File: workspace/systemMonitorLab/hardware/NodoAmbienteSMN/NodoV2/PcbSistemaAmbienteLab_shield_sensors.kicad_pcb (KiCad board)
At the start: 2 copper layers, 32 x 51 mm, 6 parts, among them J5 Molex_Sensor_BMP280, J6 Molex_Sensor_DHT22, U2 Bmp280Module, U3 DHT22

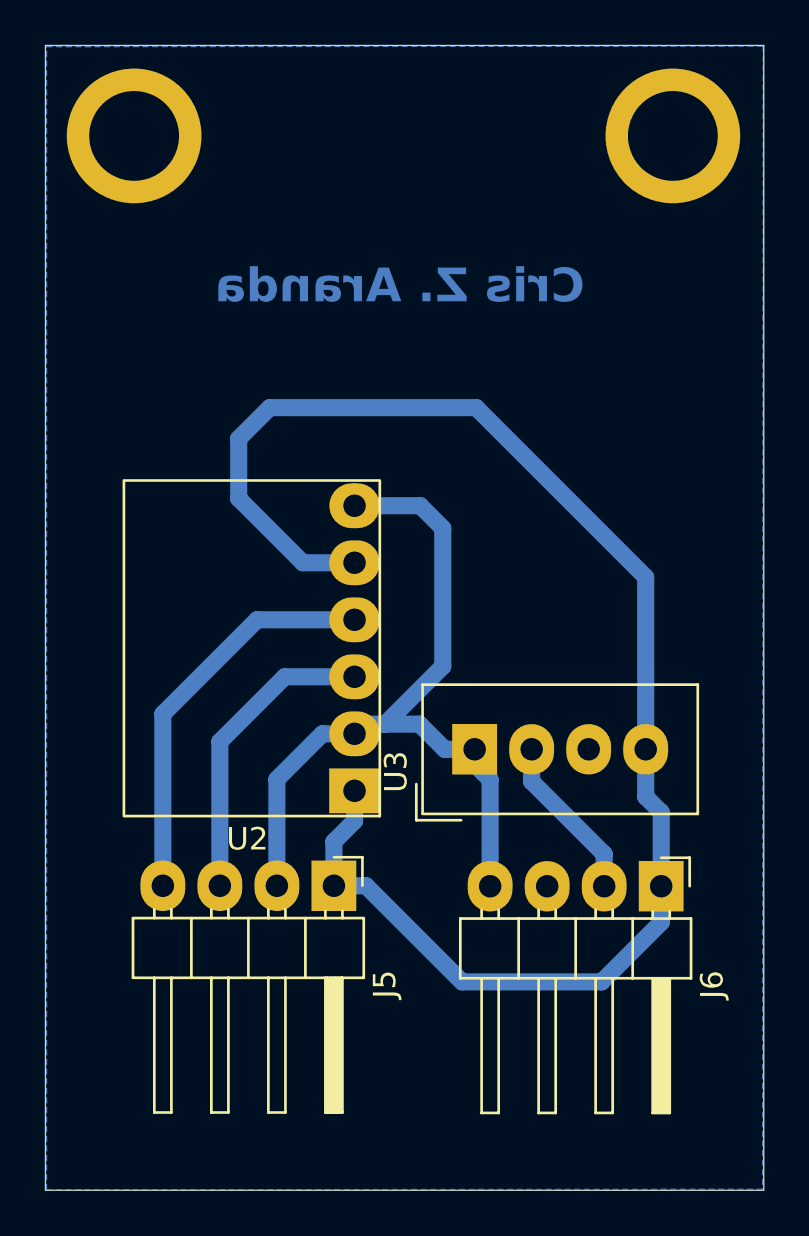
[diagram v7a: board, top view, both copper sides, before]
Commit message: Se mejora el plano de masa del PCB
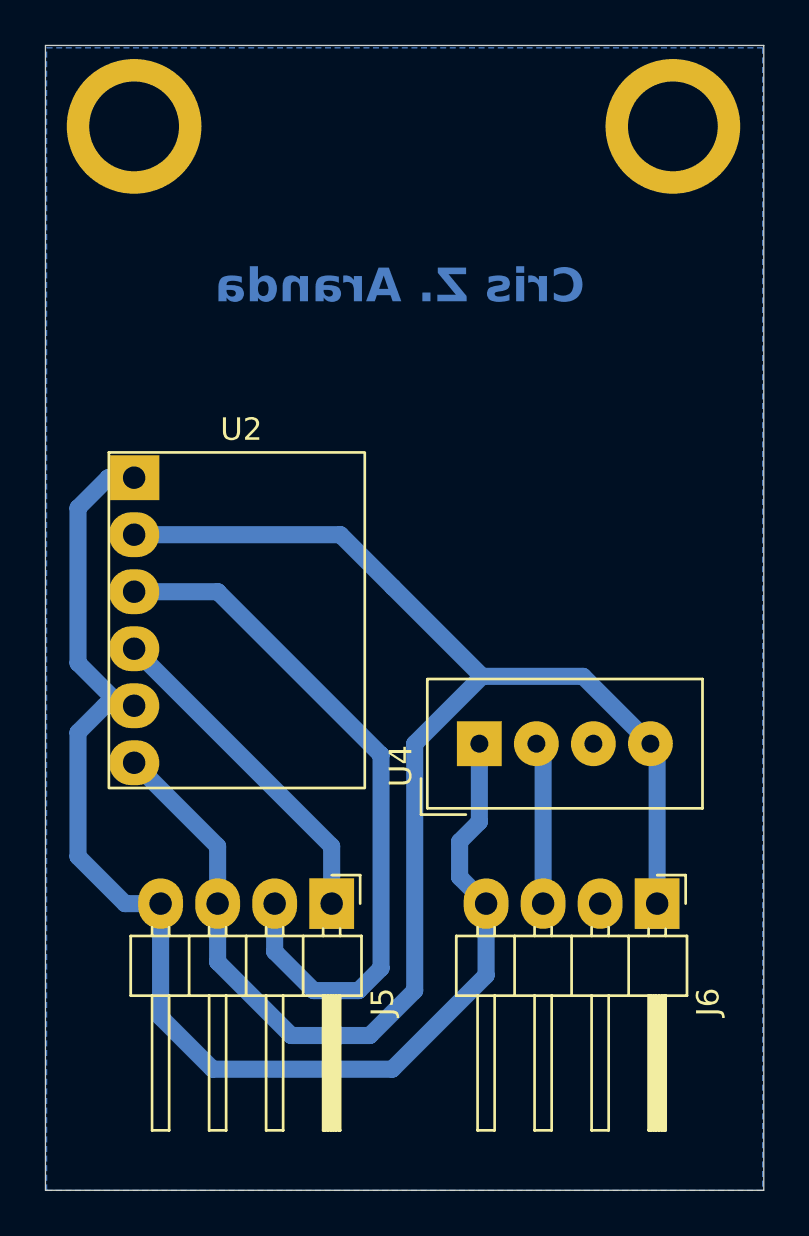
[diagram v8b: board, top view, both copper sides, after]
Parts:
- removed the ? at (180.0, 52.9)
- removed the ? at (156.0, 52.9)
- removed U3: DHT22, Sensor:Aosong_DHT11_5.5x12.0_P2.54mm
- added ?: , , F.Cu at (180.0, 52.5)
- added ?: , , F.Cu at (156.0, 52.5)
- added U4: DHT22, Sensor:Aosong_DHT11_5.5x12.0_P2.54mm, F.Cu at (171.4, 80.0)
- U2: footprint Sensors_commercial:BMP280_Module -> Modulos_comerciales:BMP280_Module
- moved U2 17.1 mm to (156.0, 68.2), turned to 0 degrees
- moved J5 0.80 mm to (164.8, 87.1)
- moved J6 0.80 mm to (179.3, 87.1)
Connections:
- J5 pad 1: 3V3 -> Net-(J5-Pin_1)
- J5 pad 2: GND -> Net-(J5-Pin_2)
- J5 pad 3: Net-(J5-Pin_3) -> GND
- J5 pad 4: Net-(J5-Pin_4) -> 3V3
- J6 pad 1: 3V3 -> GND
- J6 pad 2: Net-(J6-Pin_2) -> unconnected-(J6-Pin_2-Pad2)
- J6 pad 3: unconnected-(J6-Pin_3-Pad3) -> Net-(J6-Pin_3)
- J6 pad 4: GND -> 3V3
- U2 pad 3: Net-(J5-Pin_3) -> Net-(J5-Pin_2)
- U2 pad 4: Net-(J5-Pin_4) -> Net-(J5-Pin_1)
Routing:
- net GND: track 35.8 -> 70.7 mm
- net Net-(J5-Pin_2): track 0.00 -> 31.5 mm
- net Net-(J5-Pin_4): track 17.9 -> 0.00 mm
- net Net-(J5-Pin_1): track 0.00 -> 15.0 mm
- net Net-(J5-Pin_3): track 13.6 -> 0.00 mm
- net 3V3: track 68.6 -> 59.7 mm
- net Net-(J6-Pin_2): track 7.44 -> 0.00 mm
- net Net-(J6-Pin_3): track 0.00 -> 7.25 mm
